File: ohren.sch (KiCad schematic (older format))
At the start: 74 parts, among them J1 Conn_01x19_Male, U1 TLC5951RHA

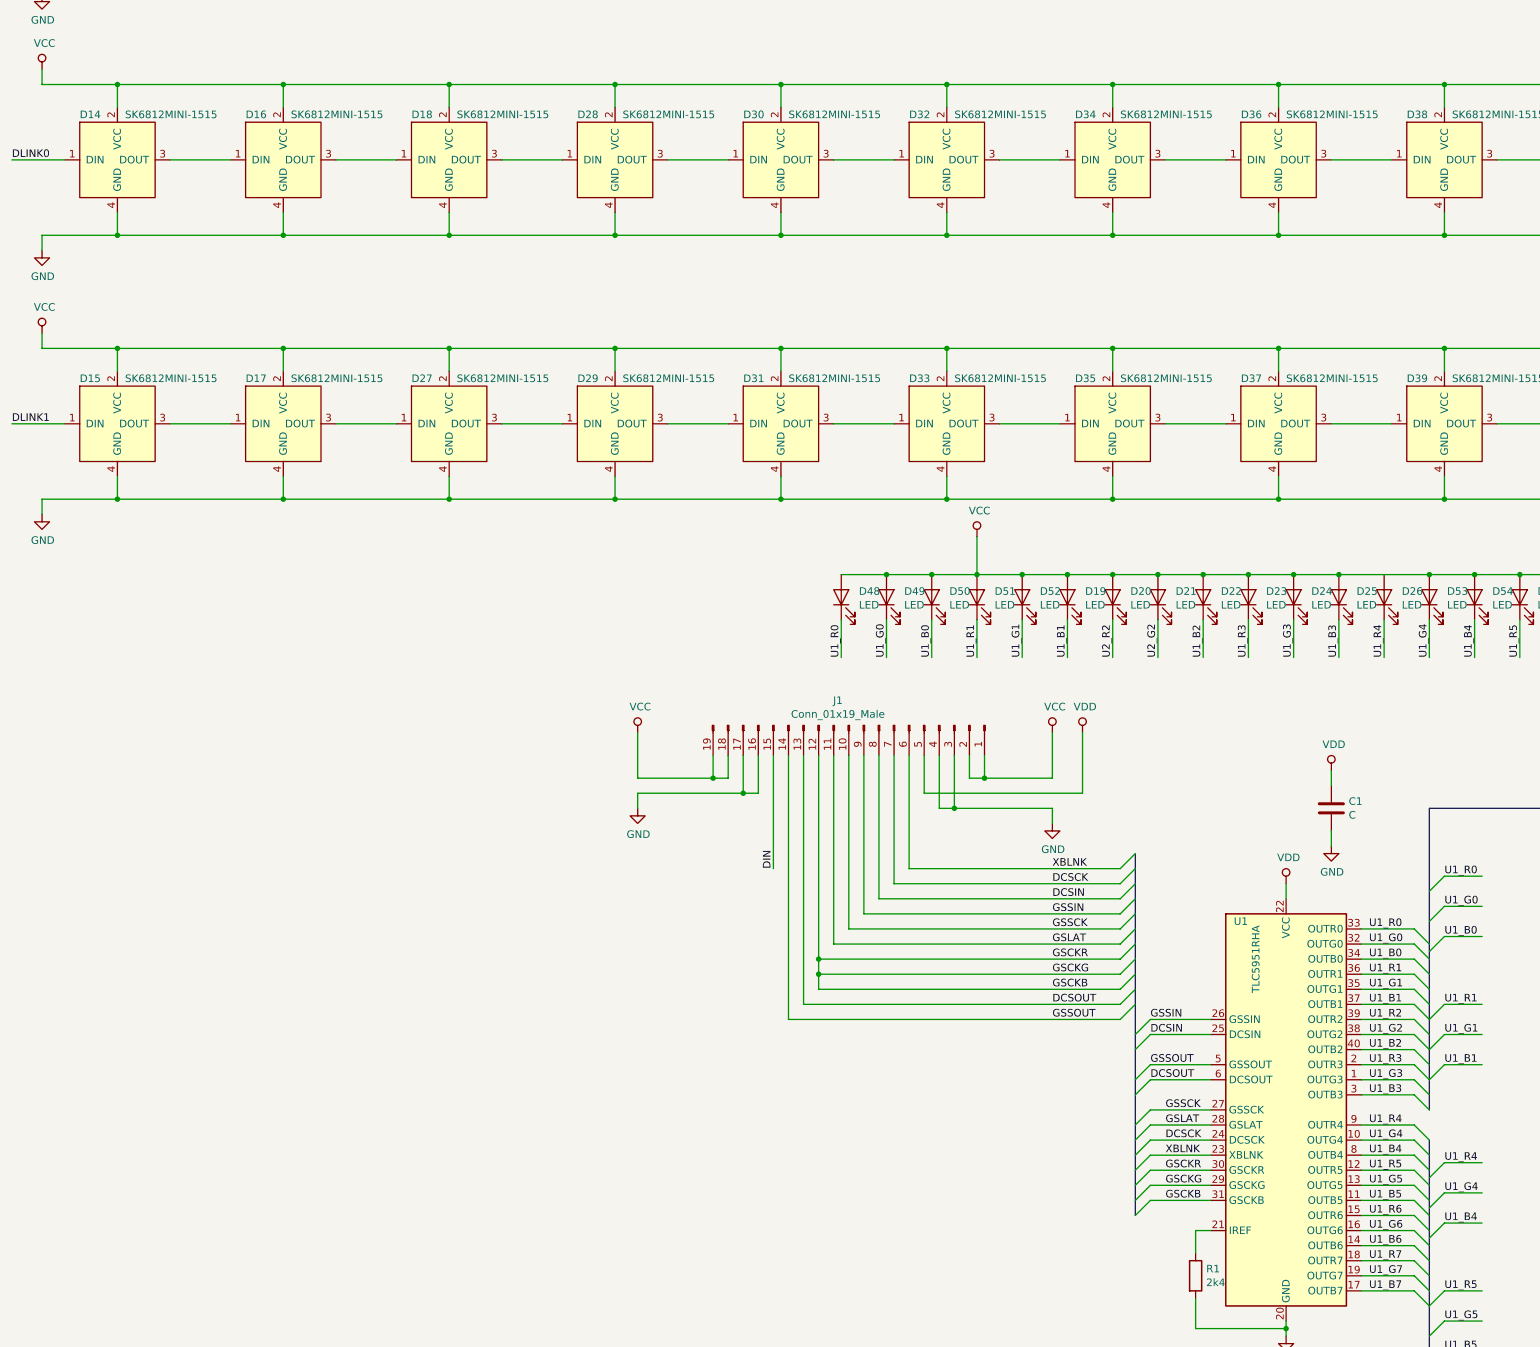
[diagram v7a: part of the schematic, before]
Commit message: Route new layout
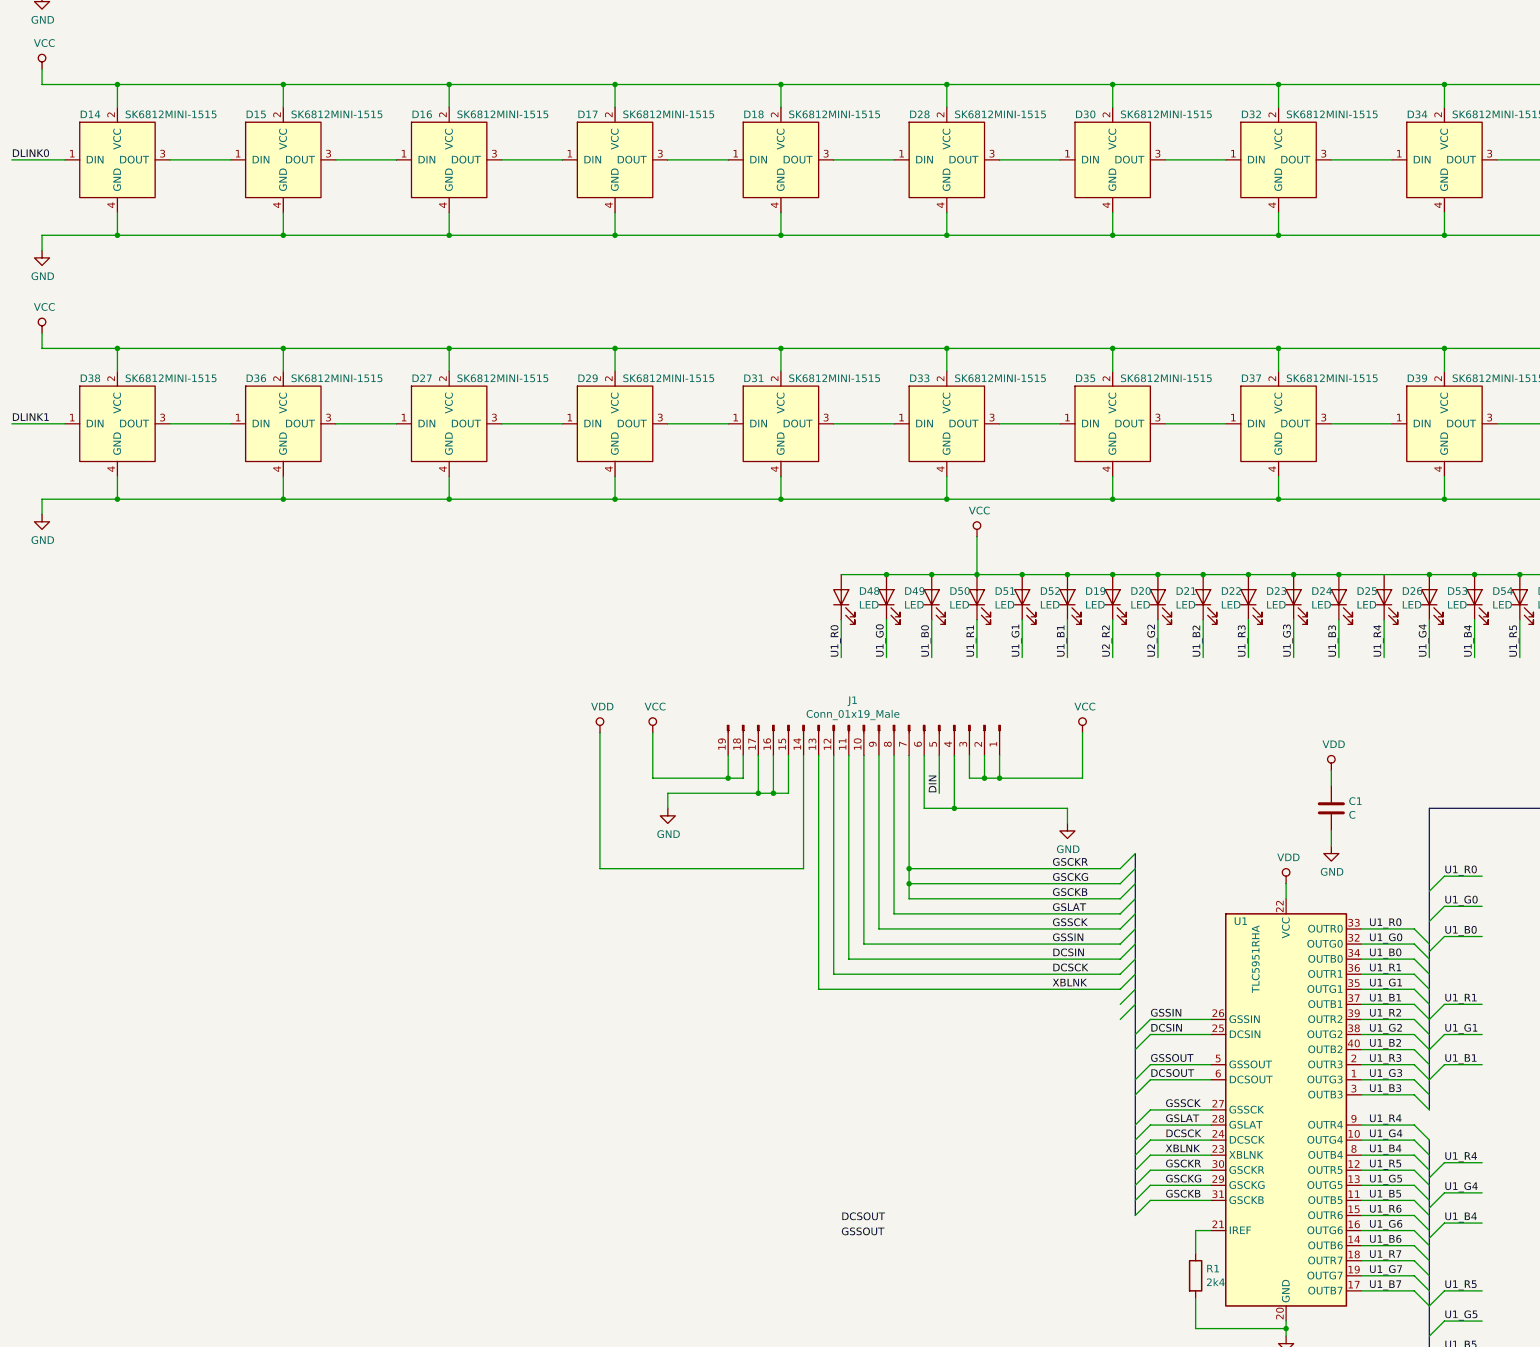
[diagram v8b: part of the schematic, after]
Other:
- moved on the sheet: D15, D16, D17, D18, D28, D30, D32, D34, D36, D38, J1
